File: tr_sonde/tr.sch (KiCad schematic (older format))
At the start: 85 parts, among them J1 SMA, J2 SMA, J3 SMA, K1 TR, K2 HV_MON, K3 VINHDR, K4 TR, Q1 PBSS4250X, Q2 MMBT2222A, Q3 STD2NK90ZT4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

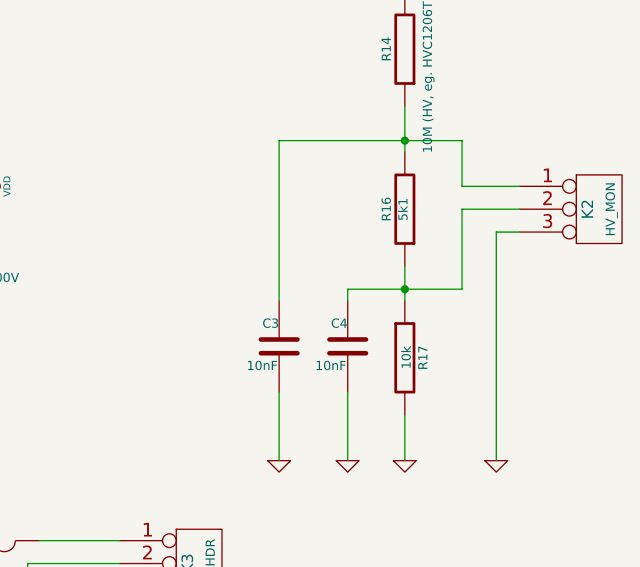
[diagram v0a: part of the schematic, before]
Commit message: updated resistor values in power supply monitoring circuit
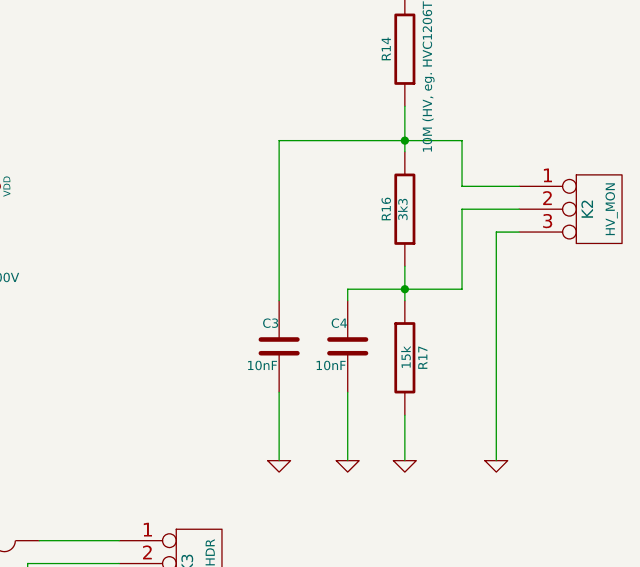
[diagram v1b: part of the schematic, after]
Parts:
- R16: value 5k1 -> 3k3
- R17: value 10k -> 15k
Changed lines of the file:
@@
 P 15550 1850
 F 0 "R16" V 15630 1850 40  0000 C CNN
-F 1 "5k1" V 15557 1851 40  0000 C CNN
+F 1 "3k3" V 15557 1851 40  0000 C CNN
 F 2 "smd_capacitors:c_0805" V 15480 1850 30  0001 C CNN
 F 3 "~" H 15550 1850 30  0000 C CNN
@@
 P 15550 2500
 F 0 "R17" V 15630 2500 40  0000 C CNN
-F 1 "10k" V 15557 2501 40  0000 C CNN
+F 1 "15k" V 15557 2501 40  0000 C CNN
 F 2 "smd_capacitors:c_0805" V 15480 2500 30  0001 C CNN
 F 3 "~" H 15550 2500 30  0000 C CNN

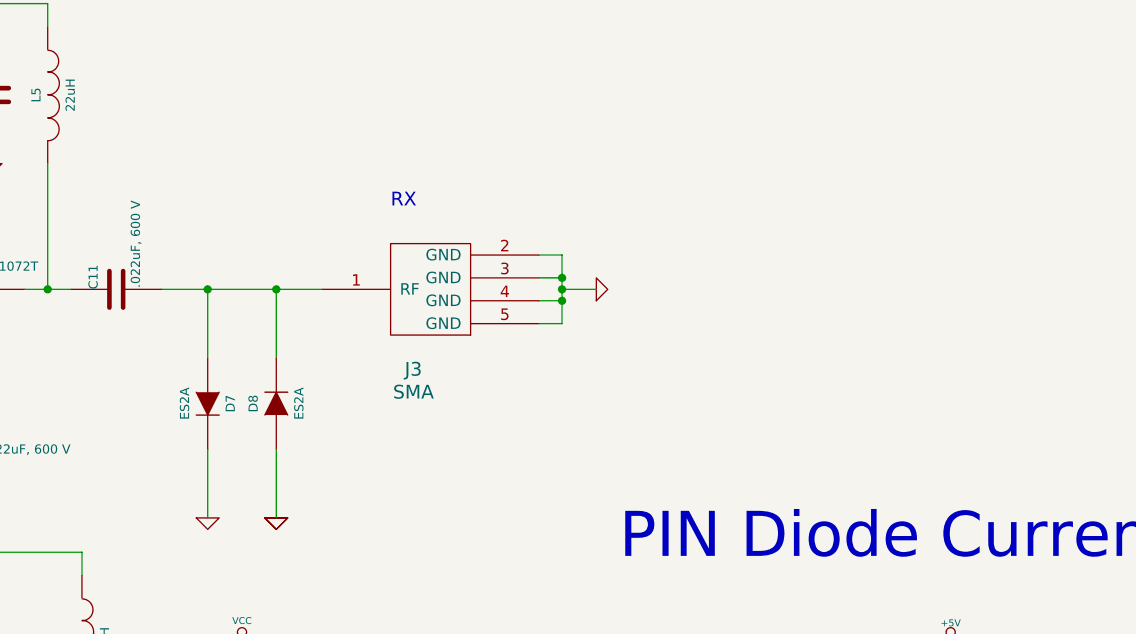
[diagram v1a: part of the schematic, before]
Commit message: moved rf amps from control board to rxfe and driver
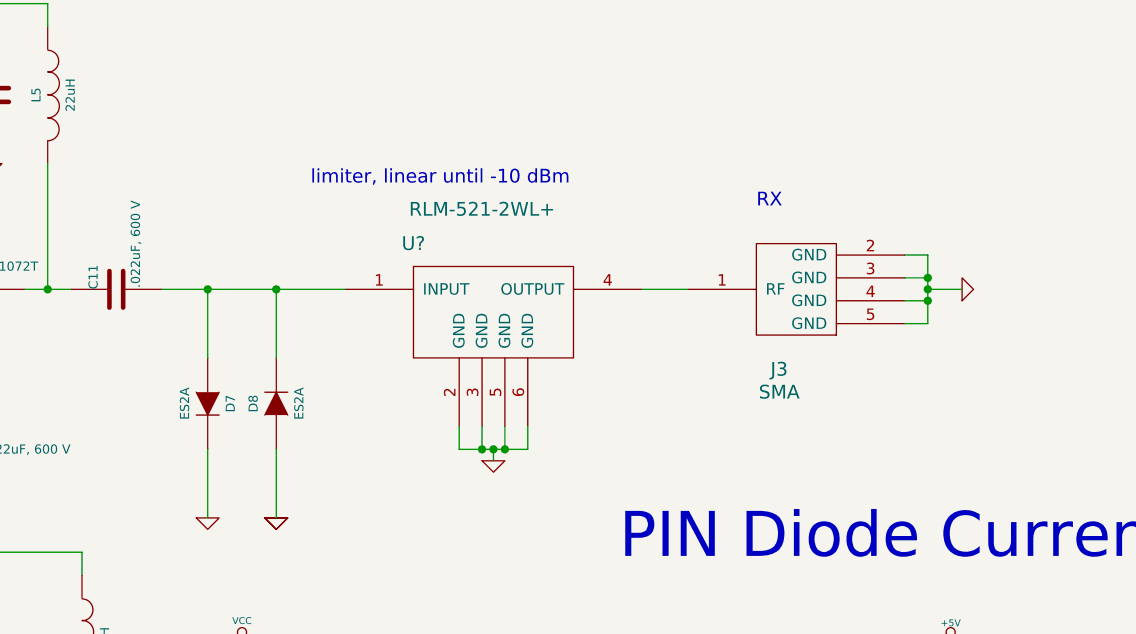
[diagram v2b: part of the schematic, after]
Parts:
- added U?: RLM-521-2WL+, symbol RLM-521-2WL+
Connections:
- net GND: now also U?.2 (GND), U?.3 (GND), U?.5 (GND), U?.6 (GND)
- net at C11.2, D7.1 (A), D8.2 (K): now also U?.1 (INPUT); no longer J3.1 (RF)
- new net: J3.1 (RF), U?.4 (OUTPUT)
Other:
- note added: "limiter, linear until -10 dBm"
- moved on the sheet: J3

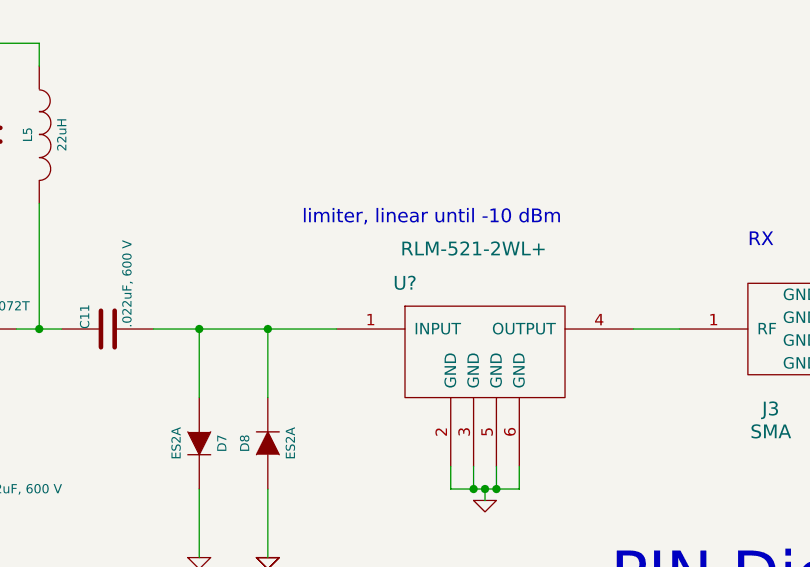
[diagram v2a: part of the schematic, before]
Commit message: added footprint for smd limiter
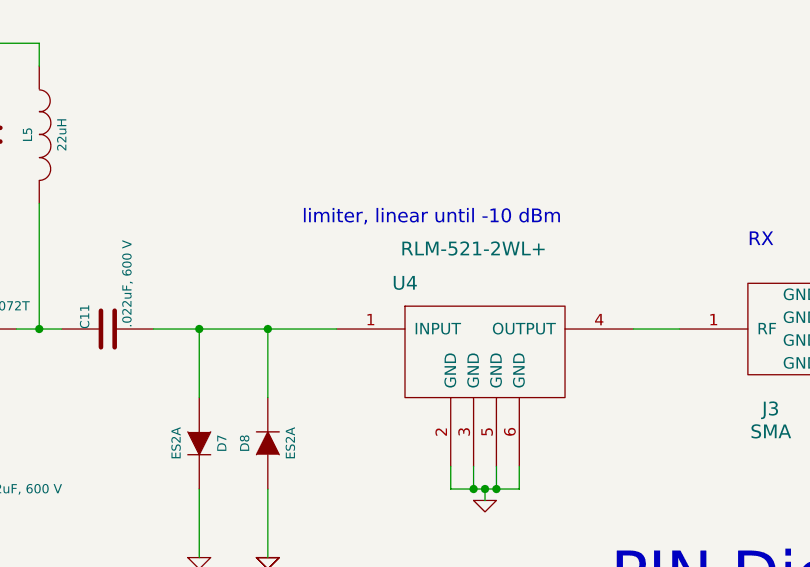
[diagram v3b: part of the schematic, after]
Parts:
- gave numbers to parts that had none: 1
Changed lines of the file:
@@
 $EndComp
 $Comp
-L GND #PWR30
+L GND #PWR34
 U 1 1 52AA0DB5
 P 10950 5800
-F 0 "#PWR30" H 10950 5800 30  0001 C CNN
+F 0 "#PWR34" H 10950 5800 30  0001 C CNN
 F 1 "GND" H 10950 5730 30  0001 C CNN
 F 2 "" H 10950 5800 60  0000 C CNN
@@
 $EndComp
 $Comp
-L GND #PWR57
+L GND #PWR58
 U 1 1 52ABD1A1
 P 15400 6350
-F 0 "#PWR57" H 15400 6350 30  0001 C CNN
+F 0 "#PWR58" H 15400 6350 30  0001 C CNN
 F 1 "GND" H 15400 6280 30  0001 C CNN
 F 2 "" H 15400 6350 60  0000 C CNN
@@
 $EndComp
 $Comp
-L VDD #PWR50
+L VDD #PWR51
 U 1 1 52AE853D
 P 13700 1750
-F 0 "#PWR50" H 13700 1850 30  0001 C CNN
+F 0 "#PWR51" H 13700 1850 30  0001 C CNN
 F 1 "VDD" H 13700 1860 30  0000 C CNN
 F 2 "" H 13700 1750 60  0000 C CNN
@@
 $EndComp
 $Comp
-L GND #PWR47
+L GND #PWR48
 U 1 1 52AE8701
 P 13150 2500
-F 0 "#PWR47" H 13150 2500 30  0001 C CNN
+F 0 "#PWR48" H 13150 2500 30  0001 C CNN
 F 1 "GND" H 13150 2430 30  0001 C CNN
 F 2 "" H 13150 2500 60  0000 C CNN
@@
 $EndComp
 $Comp
-L GND #PWR48
+L GND #PWR49
 U 1 1 52AF5346
 P 13250 4250
-F 0 "#PWR48" H 13250 4250 30  0001 C CNN
+F 0 "#PWR49" H 13250 4250 30  0001 C CNN
 F 1 "GND" H 13250 4180 30  0001 C CNN
 F 2 "" H 13250 4250 60  0000 C CNN
@@
 $EndComp
 $Comp
-L GND #PWR63
+L GND #PWR64
 U 1 1 52AF5793
 P 15700 7300
-F 0 "#PWR63" H 15700 7300 30  0001 C CNN
+F 0 "#PWR64" H 15700 7300 30  0001 C CNN
 F 1 "GND" H 15700 7230 30  0001 C CNN
 F 2 "" H 15700 7300 60  0000 C CNN
@@
 $EndComp
 $Comp
-L GND #PWR45
+L GND #PWR46
 U 1 1 52AF5977
 P 13000 4250
-F 0 "#PWR45" H 13000 4250 30  0001 C CNN
+F 0 "#PWR46" H 13000 4250 30  0001 C CNN
 F 1 "GND" H 13000 4180 30  0001 C CNN
 F 2 "" H 13000 4250 60  0000 C CNN
@@
 $EndComp
 $Comp
-L GND #PWR42
+L GND #PWR43
 U 1 1 52AF597D
 P 12750 4250
-F 0 "#PWR42" H 12750 4250 30  0001 C CNN
+F 0 "#PWR43" H 12750 4250 30  0001 C CNN
 F 1 "GND" H 12750 4180 30  0001 C CNN
 F 2 "" H 12750 4250 60  0000 C CNN
@@
 $EndComp
 $Comp
-L GND #PWR51
+L GND #PWR52
 U 1 1 53376FDF
 P 13900 3550
-F 0 "#PWR51" H 13900 3550 30  0001 C CNN
+F 0 "#PWR52" H 13900 3550 30  0001 C CNN
 F 1 "GND" H 13900 3480 30  0001 C CNN
 F 2 "" H 13900 3550 60  0000 C CNN
@@
 $EndComp
 $Comp
-L VCC #PWR41
+L VCC #PWR42
 U 1 1 5337703B
 P 12750 2900
-F 0 "#PWR41" H 12750 3000 30  0001 C CNN
+F 0 "#PWR42" H 12750 3000 30  0001 C CNN
 F 1 "VCC" H 12750 3000 30  0000 C CNN
 F 2 "" H 12750 2900 60  0000 C CNN
@@
 $EndComp
 $Comp
-L GND #PWR36
+L GND #PWR37
 U 1 1 53484265
 P 11350 2500
-F 0 "#PWR36" H 11350 2500 30  0001 C CNN
+F 0 "#PWR37" H 11350 2500 30  0001 C CNN
 F 1 "GND" H 11350 2430 30  0001 C CNN
 F 2 "" H 11350 2500 60  0000 C CNN
@@
 $EndComp
 $Comp
-L GND #PWR37
+L GND #PWR38
 U 1 1 534843BD
 P 11700 2500
-F 0 "#PWR37" H 11700 2500 30  0001 C CNN
+F 0 "#PWR38" H 11700 2500 30  0001 C CNN
 F 1 "GND" H 11700 2430 30  0001 C CNN
 F 2 "" H 11700 2500 60  0000 C CNN
@@
 $EndComp
 $Comp
-L GND #PWR34
+L GND #PWR35
 U 1 1 537E5711
 P 11100 8100
-F 0 "#PWR34" H 11100 8100 30  0001 C CNN
+F 0 "#PWR35" H 11100 8100 30  0001 C CNN
 F 1 "GND" H 11100 8030 30  0001 C CNN
 F 2 "" H 11100 8100 60  0000 C CNN
@@
 $EndComp
 $Comp
-L +5V #PWR62
+L +5V #PWR63
 U 1 1 537E5D07
 P 15700 5400
-F 0 "#PWR62" H 15700 5490 20  0001 C CNN
+F 0 "#PWR63" H 15700 5490 20  0001 C CNN
 F 1 "+5V" H 15700 5490 30  0000 C CNN
 F 2 "" H 15700 5400 60  0000 C CNN
@@
 $EndComp
 $Comp
-L GND #PWR40
+L GND #PWR41
 U 1 1 537E7018
 P 12400 5600
-F 0 "#PWR40" H 12400 5600 30  0001 C CNN
+F 0 "#PWR41" H 12400 5600 30  0001 C CNN
 F 1 "GND" H 12400 5530 30  0001 C CNN
 F 2 "" H 12400 5600 60  0000 C CNN
@@
 $EndComp
 $Comp
-L GND #PWR39
+L GND #PWR40
 U 1 1 537E737F
 P 12100 5600
-F 0 "#PWR39" H 12100 5600 30  0001 C CNN
+F 0 "#PWR40" H 12100 5600 30  0001 C CNN
 F 1 "GND" H 12100 5530 30  0001 C CNN
 F 2 "" H 12100 5600 60  0000 C CNN
@@
 $EndComp
 $Comp
-L GND #PWR29
+L GND #PWR30
 U 1 1 537E74F6
 P 9300 1550
-F 0 "#PWR29" H 9300 1550 30  0001 C CNN
+F 0 "#PWR30" H 9300 1550 30  0001 C CNN
 F 1 "GND" H 9300 1480 30  0001 C CNN
 F 2 "" H 9300 1550 60  0000 C CNN
@@
 $EndComp
 $Comp
-L GND #PWR27
+L GND #PWR28
 U 1 1 537E78FB
 P 9100 2900
-F 0 "#PWR27" H 9100 2900 30  0001 C CNN
+F 0 "#PWR28" H 9100 2900 30  0001 C CNN
 F 1 "GND" H 9100 2830 30  0001 C CNN
 F 2 "" H 9100 2900 60  0000 C CNN
@@
 $EndComp
 $Comp
-L GND #PWR49
+L GND #PWR50
 U 1 1 537E9221
 P 13500 2550
-F 0 "#PWR49" H 13500 2550 30  0001 C CNN
+F 0 "#PWR50" H 13500 2550 30  0001 C CNN
 F 1 "GND" H 13500 2480 30  0001 C CNN
 F 2 "" H 13500 2550 60  0000 C CNN
@@
 $EndComp
 $Comp
-L VCC #PWR28
+L VCC #PWR29
 U 1 1 537F9103
 P 9200 7600
-F 0 "#PWR28" H 9200 7700 30  0001 C CNN
+F 0 "#PWR29" H 9200 7700 30  0001 C CNN
 F 1 "VCC" H 9200 7700 30  0000 C CNN
 F 2 "" H 9200 7600 60  0000 C CNN
@@
 $EndComp
 $Comp
-L VCC #PWR35
+L VCC #PWR36
 U 1 1 537F913B
 P 11200 9450
-F 0 "#PWR35" H 11200 9550 30  0001 C CNN
+F 0 "#PWR36" H 11200 9550 30  0001 C CNN
 F 1 "VCC" H 11200 9550 30  0000 C CNN
 F 2 "" H 11200 9450 60  0000 C CNN
@@
 $EndComp
 $Comp
-L VDD #PWR58
+L VDD #PWR59
 U 1 1 537FA30C
 P 15550 750
-F 0 "#PWR58" H 15550 850 30  0001 C CNN
+F 0 "#PWR59" H 15550 850 30  0001 C CNN
 F 1 "VDD" H 15550 860 30  0000 C CNN
 F 2 "" H 15550 750 60  0000 C CNN
@@
 $EndComp
 $Comp
-L GND #PWR59
+L GND #PWR60
 U 1 1 537FA865
 P 15550 2950
-F 0 "#PWR59" H 15550 2950 30  0001 C CNN
+F 0 "#PWR60" H 15550 2950 30  0001 C CNN
 F 1 "GND" H 15550 2880 30  0001 C CNN
 F 2 "" H 15550 2950 60  0000 C CNN
@@
 $EndComp
 $Comp
-L GND #PWR64
+L GND #PWR65
 U 1 1 537FAD00
 P 15950 2950
-F 0 "#PWR64" H 15950 2950 30  0001 C CNN
+F 0 "#PWR65" H 15950 2950 30  0001 C CNN
 F 1 "GND" H 15950 2880 30  0001 C CNN
 F 2 "" H 15950 2950 60  0000 C CNN
@@
 $EndComp
 $Comp
-L VCC #PWR52
+L VCC #PWR53
 U 1 1 537FAE62
 P 14200 6300
-F 0 "#PWR52" H 14200 6400 30  0001 C CNN
+F 0 "#PWR53" H 14200 6400 30  0001 C CNN
 F 1 "VCC" H 14200 6400 30  0000 C CNN
 F 2 "" H 14200 6300 60  0000 C CNN
@@
 $EndComp
 $Comp
-L GND #PWR53
+L GND #PWR54
 U 1 1 537FB0A2
 P 14200 7800
-F 0 "#PWR53" H 14200 7800 30  0001 C CNN
+F 0 "#PWR54" H 14200 7800 30  0001 C CNN
 F 1 "GND" H 14200 7730 30  0001 C CNN
 F 2 "" H 14200 7800 60  0000 C CNN
@@
 $EndComp
 $Comp
-L GND #PWR54
+L GND #PWR55
 U 1 1 537FB41D
 P 14550 7800
-F 0 "#PWR54" H 14550 7800 30  0001 C CNN
+F 0 "#PWR55" H 14550 7800 30  0001 C CNN
 F 1 "GND" H 14550 7730 30  0001 C CNN
 F 2 "" H 14550 7800 60  0000 C CNN
@@
 $EndComp
 $Comp
-L +5V #PWR43
+L +5V #PWR44
 U 1 1 5384E820
 P 12750 4650
-F 0 "#PWR43" H 12750 4740 20  0001 C CNN
+F 0 "#PWR44" H 12750 4740 20  0001 C CNN
 F 1 "+5V" H 12750 4740 30  0000 C CNN
 F 2 "" H 12750 4650 60  0000 C CNN
@@
 $EndComp
 $Comp
-L GND #PWR46
+L GND #PWR47
 U 1 1 5384F0ED
 P 13000 5600
-F 0 "#PWR46" H 13000 5600 30  0001 C CNN
+F 0 "#PWR47" H 13000 5600 30  0001 C CNN
 F 1 "GND" H 13000 5530 30  0001 C CNN
 F 2 "" H 13000 5600 60  0000 C CNN
@@
 $EndComp
 $Comp
-L GND #PWR44
+L GND #PWR45
 U 1 1 5384F0F3
 P 12750 5600
-F 0 "#PWR44" H 12750 5600 30  0001 C CNN
+F 0 "#PWR45" H 12750 5600 30  0001 C CNN
 F 1 "GND" H 12750 5530 30  0001 C CNN
 F 2 "" H 12750 5600 60  0000 C CNN
@@
 $EndComp
 $Comp
-L GND #PWR56
+L GND #PWR57
 U 1 1 53D1771A
 P 15300 2950
-F 0 "#PWR56" H 15300 2950 30  0001 C CNN
+F 0 "#PWR57" H 15300 2950 30  0001 C CNN
 F 1 "GND" H 15300 2880 30  0001 C CNN
 F 2 "" H 15300 2950 60  0000 C CNN
@@
 $EndComp
 $Comp
-L GND #PWR55
+L GND #PWR56
 U 1 1 53D17725
 P 15000 2950
-F 0 "#PWR55" H 15000 2950 30  0001 C CNN
+F 0 "#PWR56" H 15000 2950 30  0001 C CNN
 F 1 "GND" H 15000 2880 30  0001 C CNN
 F 2 "" H 15000 2950 60  0000 C CNN
@@
 $EndComp
 $Comp
-L +5V #PWR60
+L +5V #PWR61
 U 1 1 5417206B
 P 15700 4100
-F 0 "#PWR60" H 15700 4190 20  0001 C CNN
+F 0 "#PWR61" H 15700 4190 20  0001 C CNN
 F 1 "+5V" H 15700 4190 30  0000 C CNN
 F 2 "" H 15700 4100 60  0000 C CNN
@@
 $EndComp
 $Comp
-L VCC #PWR61
+L VCC #PWR62
 U 1 1 54172076
 P 15700 4650
-F 0 "#PWR61" H 15700 4750 30  0001 C CNN
+F 0 "#PWR62" H 15700 4750 30  0001 C CNN
 F 1 "VCC" H 15700 4750 30  0000 C CNN
 F 2 "" H 15700 4650 60  0000 C CNN
@@
 $EndComp
 $Comp
-L GND #PWR38
+L GND #PWR39
 U 1 1 54172F31
 P 12000 1200
-F 0 "#PWR38" H 12000 1200 30  0001 C CNN
+F 0 "#PWR39" H 12000 1200 30  0001 C CNN
 F 1 "GND" H 12000 1130 30  0001 C CNN
 F 2 "" H 12000 1200 60  0000 C CNN
@@
 limiter, linear until -10 dBm
 $Comp
-L RLM-521-2WL+ U?
+L RLM-521-2WL+ U4
 U 1 1 54CA9187
 P 8900 5800
-F 0 "U?" H 8550 6000 60  0000 C CNN
+F 0 "U4" H 8550 6000 60  0000 C CNN
 F 1 "RLM-521-2WL+" H 8850 6150 60  0000 C CNN
 F 2 "" H 8900 5800 60  0000 C CNN
@@
 	9550 5800 9750 5800
 $Comp
-L GND #PWR?
+L GND #PWR27
 U 1 1 54CA94E8
 P 8900 6550
-F 0 "#PWR?" H 8900 6550 30  0001 C CNN
+F 0 "#PWR27" H 8900 6550 30  0001 C CNN
 F 1 "GND" H 8900 6480 30  0001 C CNN
 F 2 "" H 8900 6550 60  0000 C CNN

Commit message: DFM changes to boards - added fiducial markers and increase paste clearance
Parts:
- removed K4: TR, Connect:PINHEAD1-3, symbol CONN_3
- added FID1, FID2, FID3: FIDUCIAL, symbol MOUNTING_HOLE
- added H1, H2, H3: MOUNTING_HOLE, symbol MOUNTING_HOLE
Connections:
- net at C34.1, R3.2, U3.4 (+OUT): no longer C33.1
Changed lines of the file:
@@
 LIBS:npn_e1
 LIBS:rlm-521-2wl+
+LIBS:mounting_hole
 LIBS:tr-cache
 EELAYER 24 0
@@
 	-1   0    0    1
 $EndComp
-$Comp
-L CONN_3 K4
-U 1 1 54172BC5
-P 12000 700
-F 0 "K4" V 11950 700 50  0000 C CNN
-F 1 "TR" V 12050 700 40  0000 C CNN
-F 2 "Connect:PINHEAD1-3" H 12000 700 60  0001 C CNN
-F 3 "~" H 12000 700 60  0000 C CNN
-	1    12000 700
-	0    1    -1   0
-$EndComp
-$Comp
-L GND #PWR39
-U 1 1 54172F31
-P 12000 1200
-F 0 "#PWR39" H 12000 1200 30  0001 C CNN
-F 1 "GND" H 12000 1130 30  0001 C CNN
-F 2 "" H 12000 1200 60  0000 C CNN
-F 3 "" H 12000 1200 60  0000 C CNN
-	1    12000 1200
-	1    0    0    -1
-$EndComp
 Text Notes 8100 5350 0    60   ~ 0
 limiter, linear until -10 dBm
@@
 	10800 1550 10950 1550
 Connection ~ 11350 1750
-Wire Wire Line
-	11350 1150 11350 1800
 Connection ~ 11700 1750
 Wire Wire Line
@@
 	15700 4100 15700 4150
 Wire Wire Line
-	11350 1150 11900 1150
-Wire Wire Line
 	11900 1150 11900 1050
-Wire Wire Line
-	12000 1200 12000 1050
 Wire Wire Line
 	9550 5800 9750 5800
@@
 	8900 6500 8900 6550
 Connection ~ 8900 6500
+$Comp
+L MOUNTING_HOLE H3
+U 1 1 54D27155
+P 1250 1600
+F 0 "H3" H 950 1650 60  0000 C CNN
+F 1 "MOUNTING_HOLE" H 1250 1750 60  0000 C CNN
+F 2 "" H 1250 1600 60  0000 C CNN
+F 3 "" H 1250 1600 60  0000 C CNN
+	1    1250 1600
+	1    0    0    -1
+$EndComp
+$Comp
+L MOUNTING_HOLE H2
+U 1 1 54D27167
+P 1200 1900
+F 0 "H2" H 900 1950 60  0000 C CNN
+F 1 "MOUNTING_HOLE" H 1200 2050 60  0000 C CNN
+F 2 "" H 1200 1900 60  0000 C CNN
+F 3 "" H 1200 1900 60  0000 C CNN
+	1    1200 1900
+	1    0    0    -1
+$EndComp
+$Comp
+L MOUNTING_HOLE H1
+U 1 1 54D27172
+P 1150 2250
+F 0 "H1" H 850 2300 60  0000 C CNN
+F 1 "MOUNTING_HOLE" H 1150 2400 60  0000 C CNN
+F 2 "" H 1150 2250 60  0000 C CNN
+F 3 "" H 1150 2250 60  0000 C CNN
+	1    1150 2250
+	1    0    0    -1
+$EndComp
+$Comp
+L MOUNTING_HOLE FID1
+U 1 1 54D2717D
+P 2000 1550
+F 0 "FID1" H 1700 1600 60  0000 C CNN
+F 1 "FIDUCIAL" H 2000 1700 60  0000 C CNN
+F 2 "" H 2000 1550 60  0000 C CNN
+F 3 "" H 2000 1550 60  0000 C CNN
+	1    2000 1550
+	1    0    0    -1
+$EndComp
+$Comp
+L MOUNTING_HOLE FID2
+U 1 1 54D27192
+P 2000 1900
+F 0 "FID2" H 1700 1950 60  0000 C CNN
+F 1 "FIDUCIAL" H 2000 2050 60  0000 C CNN
+F 2 "" H 2000 1900 60  0000 C CNN
+F 3 "" H 2000 1900 60  0000 C CNN
+	1    2000 1900
+	1    0    0    -1
+$EndComp
+$Comp
+L MOUNTING_HOLE FID3
+U 1 1 54D2719D
+P 1950 2200
+F 0 "FID3" H 1650 2250 60  0000 C CNN
+F 1 "FIDUCIAL" H 1950 2350 60  0000 C CNN
+F 2 "" H 1950 2200 60  0000 C CNN
+F 3 "" H 1950 2200 60  0000 C CNN
+	1    1950 2200
+	1    0    0    -1
+$EndComp
 $EndSCHEMATC

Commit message: rearranged high power T/R switch to place all connectors on one side for easier mounting to cases
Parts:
- added H4: MOUNTING_HOLE, Mounting_Holes:MountingHole_3-5mm, symbol MOUNTING_HOLE
- FID1, FID2, FID3: footprint (none) -> sdtransmitter:FID_1MM
- H1, H2, H3: footprint (none) -> Mounting_Holes:MountingHole_3-5mm
- K1, K2, K3: footprint Connect:PINHEAD1-3 -> sdtransmitter:0015912035
- U4: footprint (none) -> sdtransmitter:PL258
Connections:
- net at C33.1: now also C34.1, R3.2, U3.4 (+OUT)

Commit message: DFM changes..
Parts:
- removed C22, C36: 2.2uF, smd_capacitors:c_0805, symbol C
- C11, C7, C9: value .022uF, 600 V -> .022uF 600V
- C15, C2, C6: value .022uF 600 V -> .022uF 600V
- C18: value .022uF 100V -> .022uF 600V
- C28: value 100pF -> 10nF
- C33: value 4700pF 600 V -> 4700pF 600V
- D11: value GREEN -> RED
- K1: value TR -> SMDHDR
- K2: value HV_MON -> SMDHDR
- K3: value VINHDR -> SMDHDR
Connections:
- net VDD: now also R3.2; no longer R3.1
- net at C33.1, C34.1, U3.4 (+OUT): now also R3.1; no longer R3.2
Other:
- note added: "HVMON HEADER\n"
- note added: "TR HEADER"
- note added: "VIN HEADER"
